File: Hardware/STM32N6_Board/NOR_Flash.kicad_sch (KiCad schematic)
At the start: 14 parts, among them SW1 SW_Push

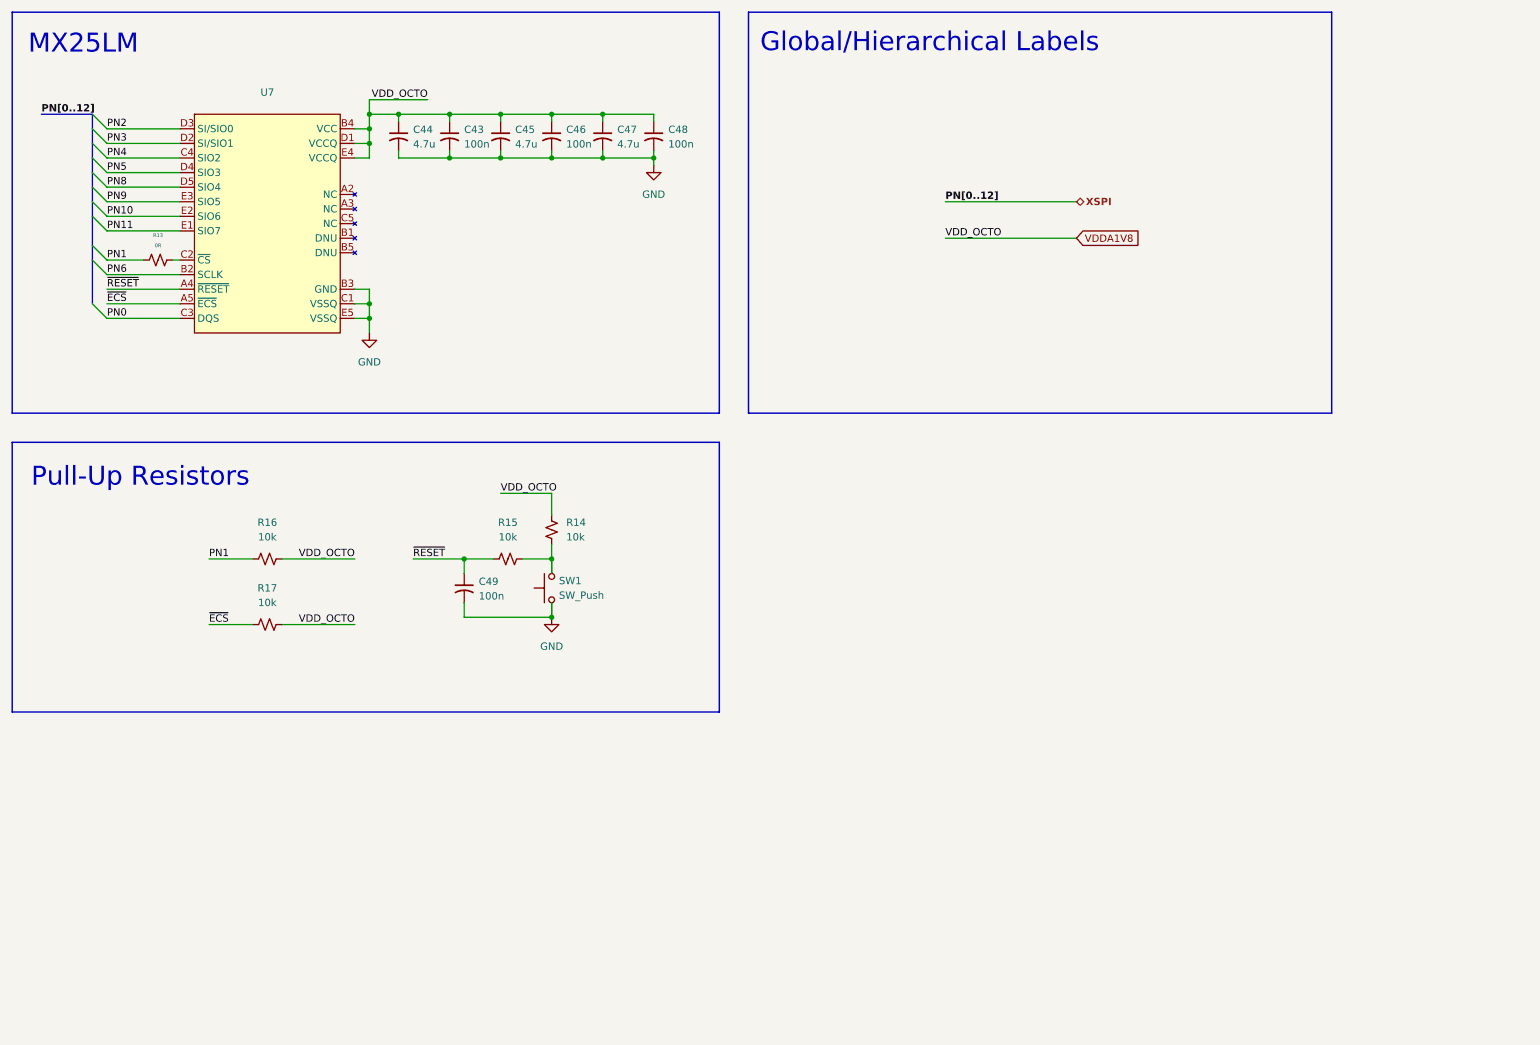
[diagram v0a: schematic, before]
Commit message: Completed wiring of the Analog unit.
- CSI and USB buses are created, yet to be connected with connectors
- Next will be pin selection, and drawing in FMC SDRAM
- Then will be routing GPIOs as buses, and connecting with connectors
- Finally, board layout.
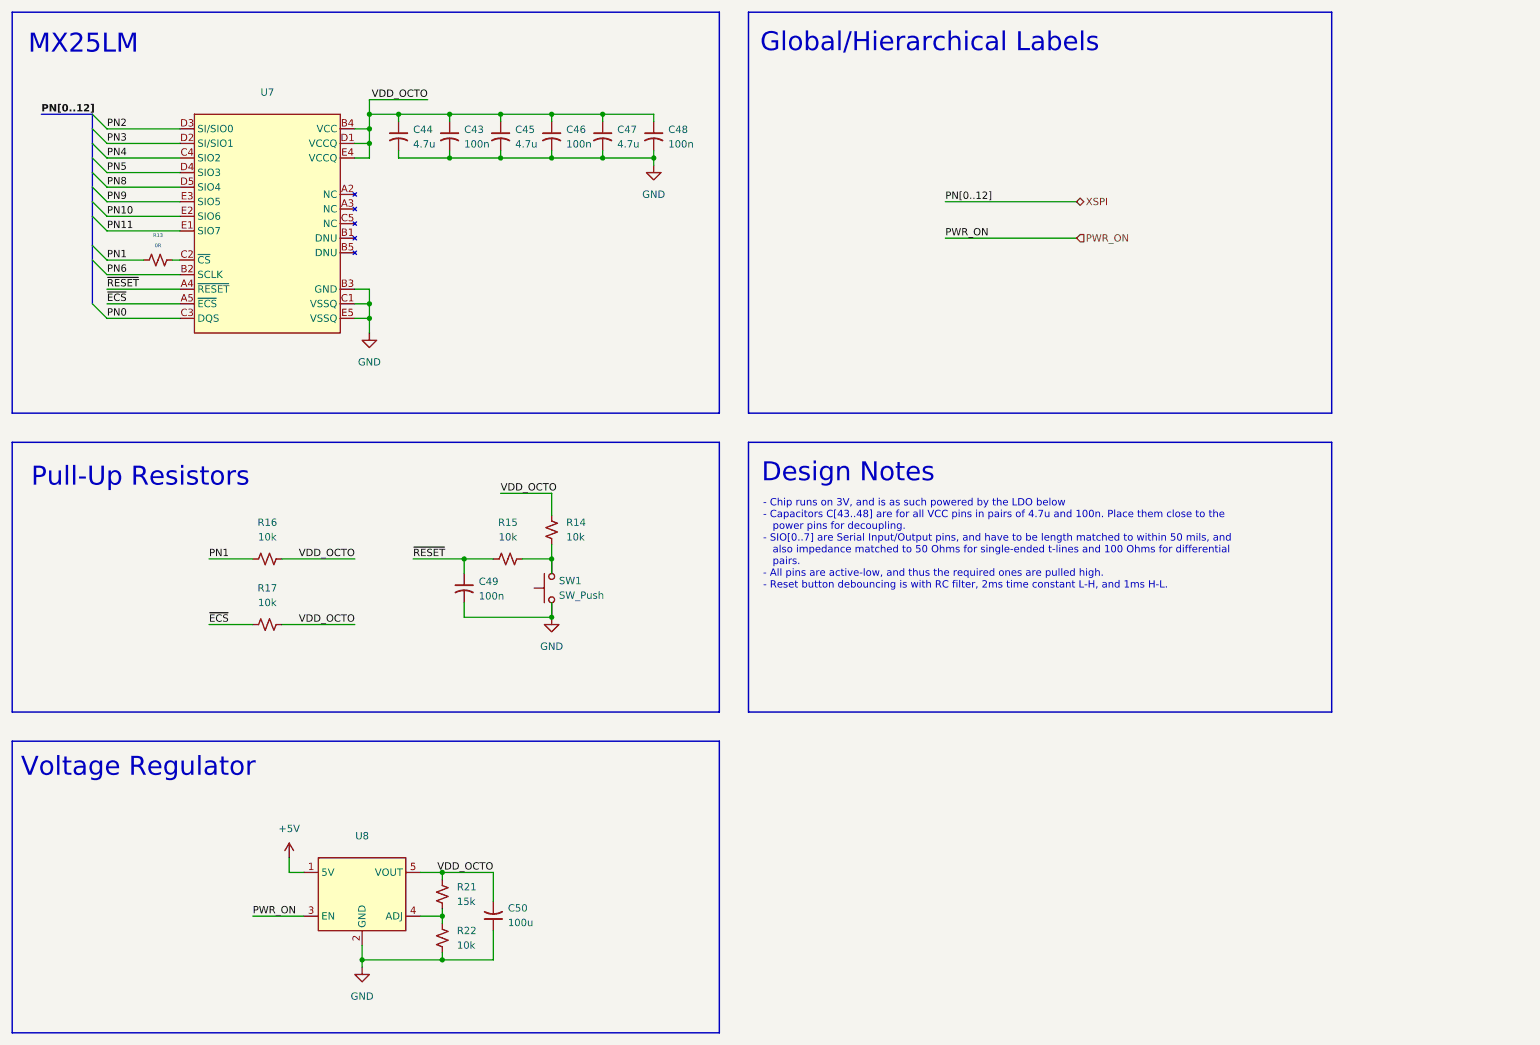
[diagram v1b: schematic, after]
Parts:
- added C50: 100u, symbol Device:C_Small_US
- added R21: 15k, symbol Device:R_Small_US
- added R22: 10k, symbol Device:R_Small_US
- added U8: ~, symbol STM32N6_Symbols:SPX5205-ADJ
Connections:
- net GND: now also C50.1, R22.2, U8.2 (GND)
- net VDDA1V8 renamed VDD_OCTO
- net VDD_OCTO: now also C50.2, R21.1, U8.5 (VOUT)
- new net: R21.2, R22.1, U8.4 (ADJ)
- new net +5V: U8.1 (5V)
- new net PWR_ON: U8.3 (EN)
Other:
- note added: "- Chip runs on 3V, and is as such powered by the LDO below - Capacitors C[43..48] are for all VCC pins in pairs of 4.7u and 100n. Place them close to the power pins for decoupling. - SIO[0..7] are Serial Input/Output pins, and have to be length matched to within 50 mils, and also impedance matched to 50 Ohms for single-ended t-lines and 100 Ohms for differential pairs. - All pins are active-low, 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"
- note added: "Design Notes"
- note added: "Voltage Regulator"

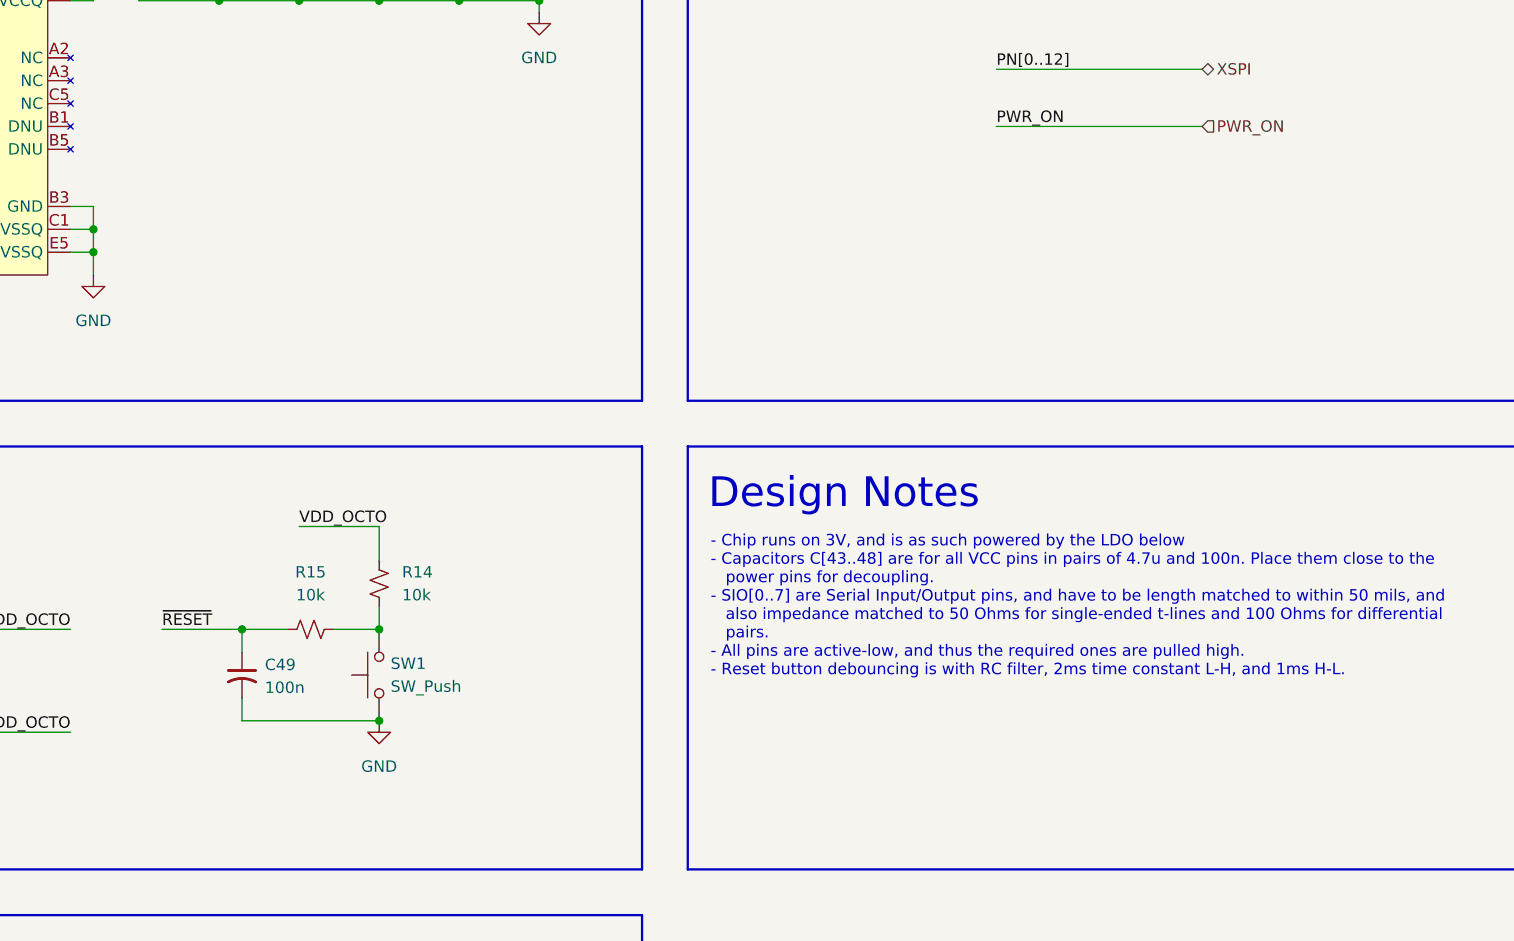
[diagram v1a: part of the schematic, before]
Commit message: Added and Updated some stuff
- Added layout guide for the IS42 SDRAM chip
- Modified reset pins wiring (now only on one reset button)
- Added design notes in docs/STM32N6/DesignNotes.md
- Updated PROGRESS.md
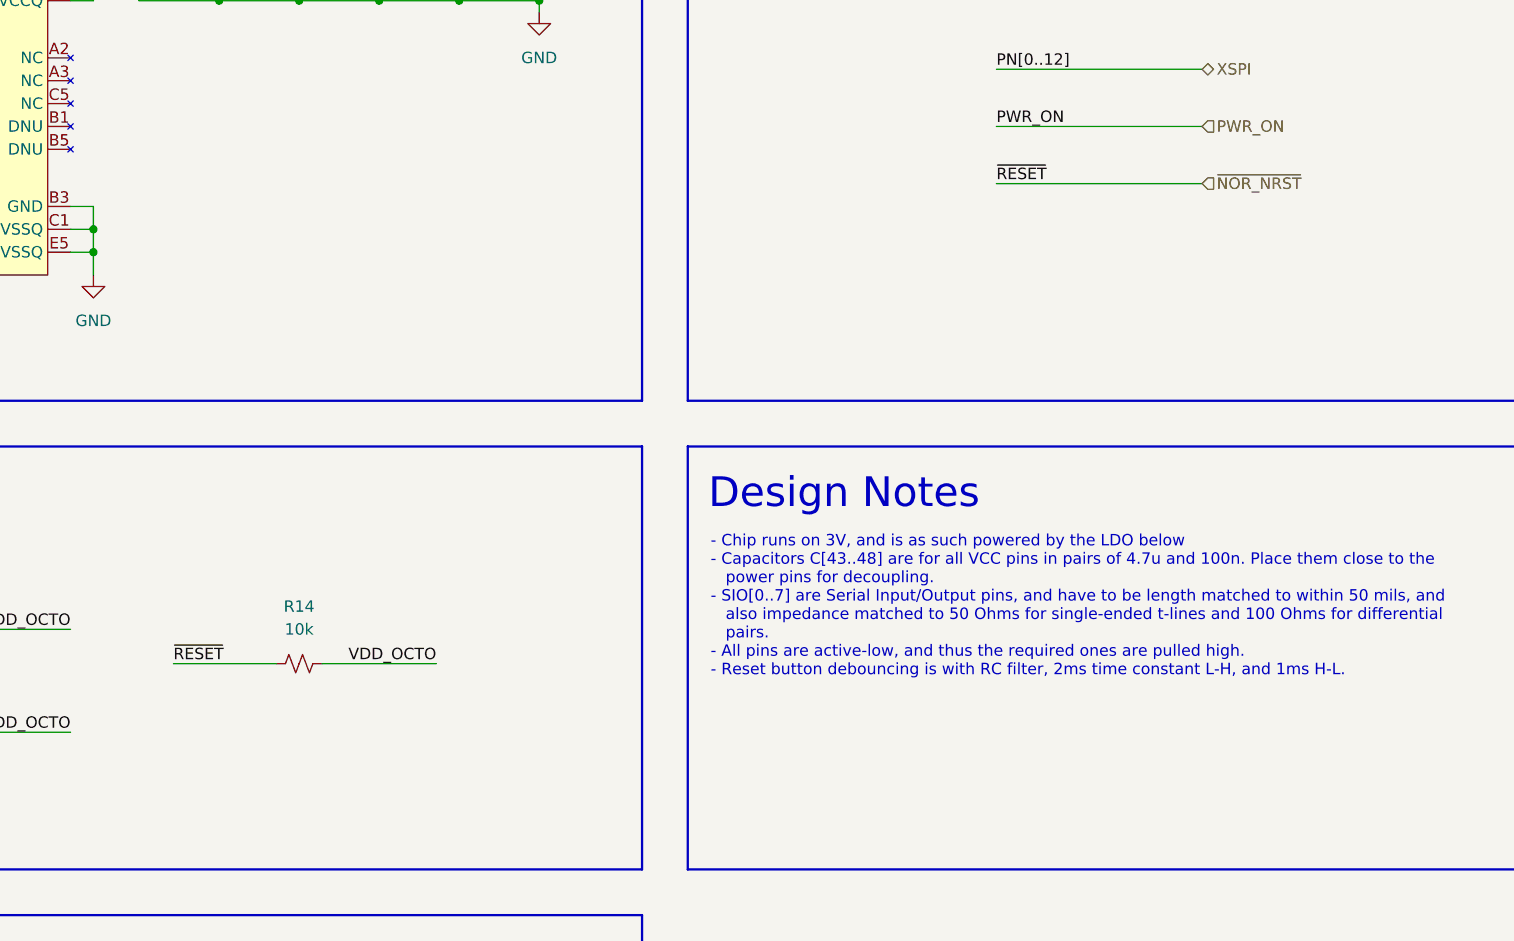
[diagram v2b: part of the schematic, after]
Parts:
- removed C49: 100n, symbol Device:C_Small_US
- removed R15: 10k, symbol Device:R_Small_US
- removed SW1: SW_Push, symbol Switch:SW_Push
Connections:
- net VDD_OCTO: now also R14.2; no longer R14.1
- net ~{RESET} renamed ~{NOR_NRST}
- net ~{NOR_NRST}: now also R14.1
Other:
- moved on the sheet: R14

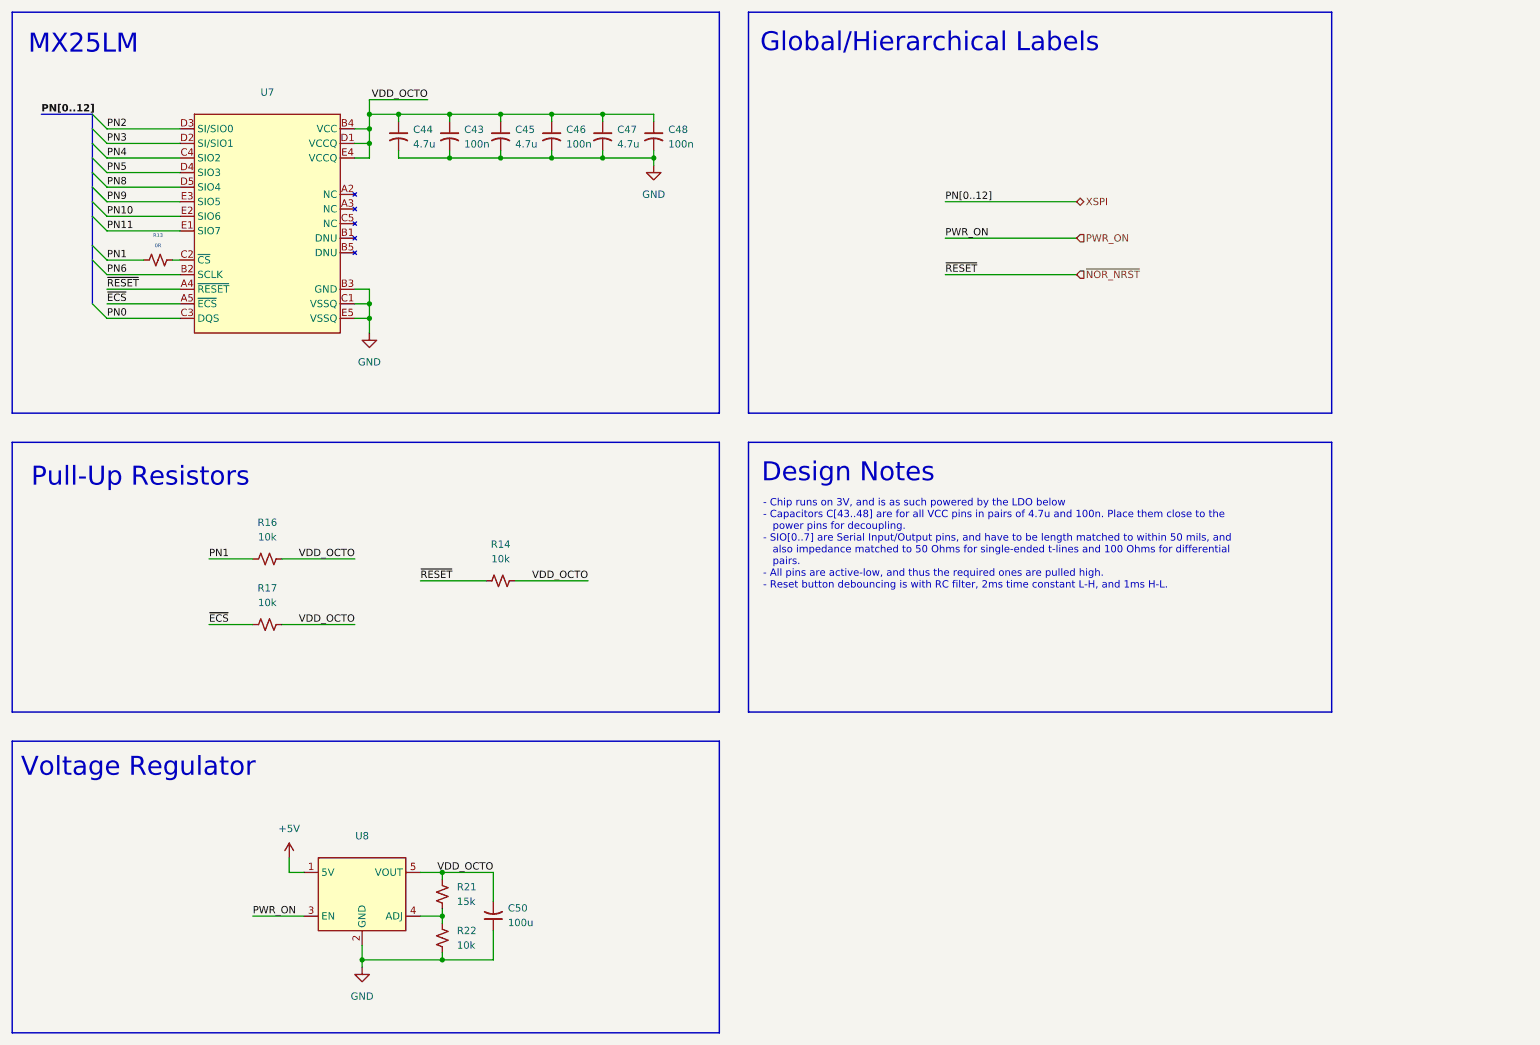
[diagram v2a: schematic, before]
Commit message: Completed the schematic.
- The schematic is complete.
- ERC checker, footprint assignment, and PCB board design left
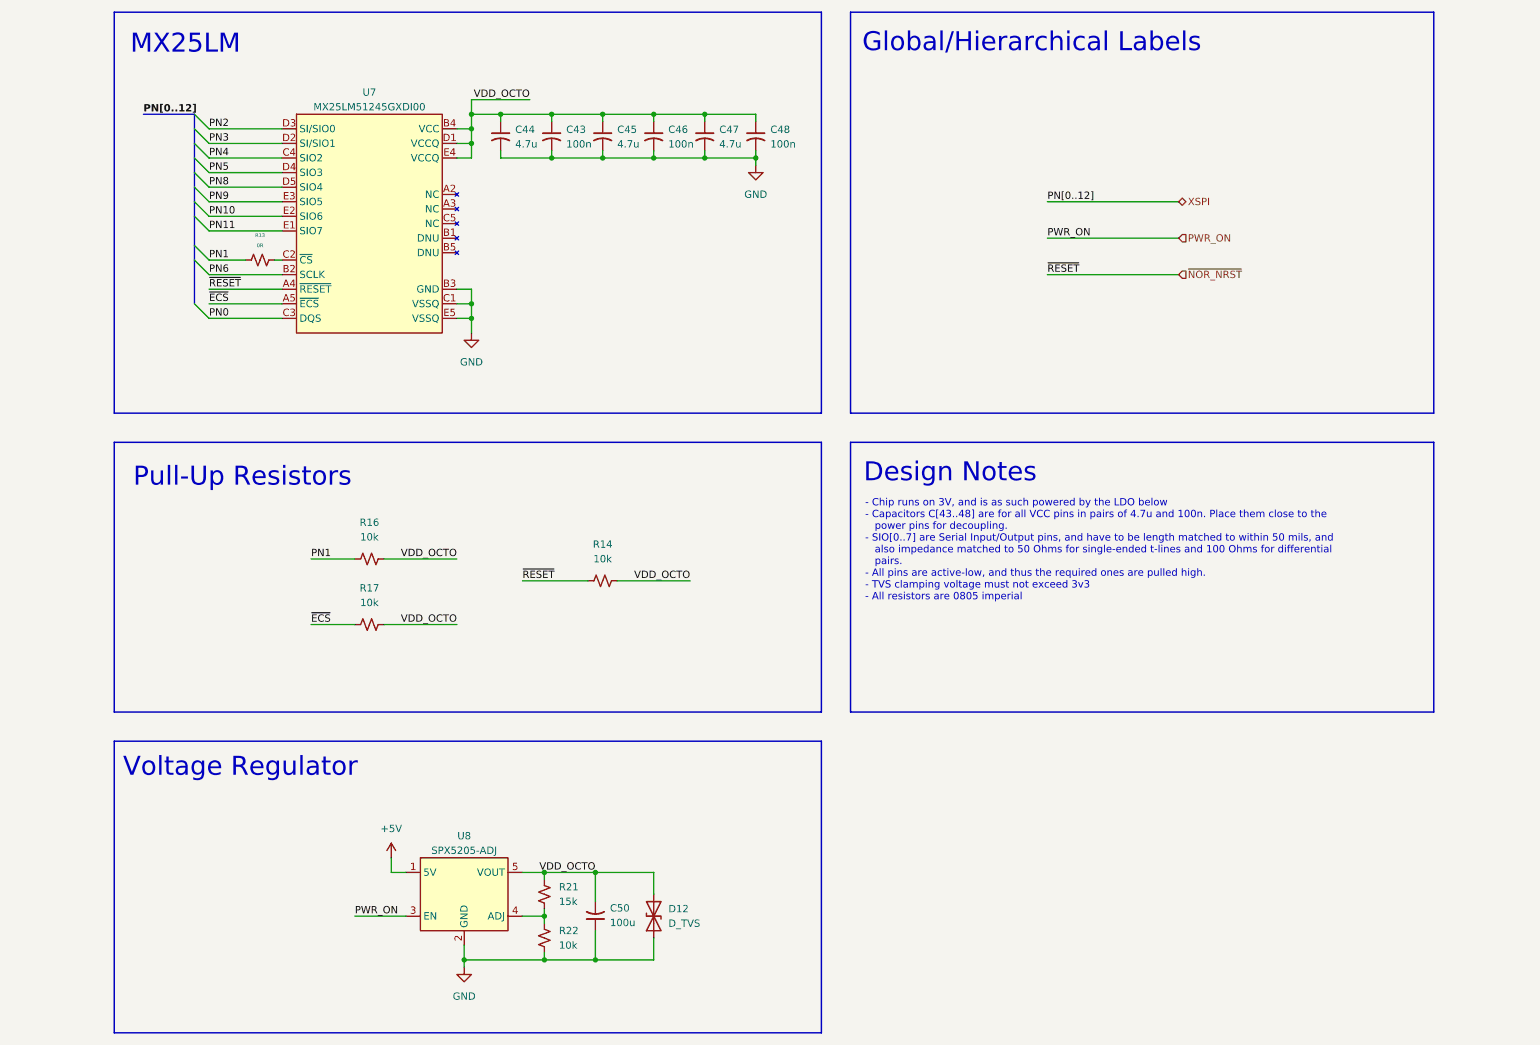
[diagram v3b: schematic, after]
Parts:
- added D12: D_TVS, symbol Device:D_TVS
- U7: value ~ -> MX25LM51245GXDI00
- U8: value ~ -> SPX5205-ADJ
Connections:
- net GND: now also D12.1 (A1)
- net VDD_OCTO: now also D12.2 (A2)
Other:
- moved on the sheet: C43, C44, C45, C46, C47, C48, C50, R13, R14, R16, R17, R21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

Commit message: Made fixes to remove ERC errors
- 1 remaining error, but > 100 warnings D:
- The remaining error is a bug within KiCAD I believe
- Next is footprint assignment
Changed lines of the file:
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@@
+		)
+	)
+	(bus
+		(pts
+			(xy 195.58 48.26) (xy 218.44 48.26)
+		)
+		(stroke
+			(width 0)
+			(type default)
 		)
 	)
@@
 		(pts
 			(xy 49.53 63.5) (xy 62.23 63.5)
-		)
-		(stroke
-			(width 0)
-			(type default)
-		)
-	)
-	(wire
-		(pts
-			(xy 195.58 48.26) (xy 218.44 48.26)
 		)
 		(stroke
@@
 		)
 	)
-	(label "PN[0..12]"
+	(label "{XSPI}"
 		(at 195.58 48.26 0)
 		(effects
@@
 		)
 	)
-	(hierarchical_label "XSPI"
+	(hierarchical_label "{XSPI}"
 		(shape bidirectional)
 		(at 218.44 48.26 0)
